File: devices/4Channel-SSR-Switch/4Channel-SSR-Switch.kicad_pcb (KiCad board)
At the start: 2 copper layers, 46 x 91.3 mm, 24 parts, among them J1 RJ45, J2 RJ45, P1 CONN_02X05, P2 CONN_01X05, P3 CONN_01X05, P4 CONN_01X05, P6 CONN_01X05, U1 LP2950, U2 STM32F030R8, U3 G3MB_SSR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

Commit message: Big cleanup/upgrade of Kicad files
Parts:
- removed G***: OSHW-logo_silkscreen-front_6mm, OSHW Logo:OSHW-logo_silkscreen-front_6mm
- added D1: SMF05C, SMF05C:SC70-6, F.Cu at (145.0, 138.8)
- added ZD1: DS9503, DS9503:TSOC6, F.Cu at (150.6, 138.2)
- moved C3 1.88 mm to (146.3, 109.5), turned to 180 degrees
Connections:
- J1 pad 1: GND -> Net-(J1-Pad1)
- J1 pad 3: GND -> Net-(J1-Pad1)
- J1 pad 4: /1W-DATA -> Net-(J1-Pad4)
- J1 pad 5: GND -> Net-(J1-Pad1)
- J1 pad 8: GND -> Net-(J1-Pad1)
- J1 pad 9: GND -> Net-(J1-Pad1)
- J2 pad 1: GND -> Net-(J1-Pad1)
- J2 pad 3: GND -> Net-(J1-Pad1)
- J2 pad 4: /1W-DATA -> Net-(J1-Pad4)
- J2 pad 5: GND -> Net-(J1-Pad1)
- J2 pad 8: GND -> Net-(J1-Pad1)
- J2 pad 9: GND -> Net-(J1-Pad1)
- P1 pad 6: (no net) -> Net-(P1-Pad6)
- P1 pad 7: (no net) -> Net-(P1-Pad7)
- P1 pad 8: (no net) -> Net-(P1-Pad8)
- U2 pad 11: (no net) -> Net-(U2-Pad11)
- U2 pad 15: (no net) -> Net-(U2-Pad15)
- U2 pad 18: (no net) -> Net-(U2-Pad18)
- U2 pad 2: (no net) -> Net-(U2-Pad2)
- U2 pad 20: (no net) -> Net-(U2-Pad20)
- U2 pad 22: (no net) -> Net-(U2-Pad22)
- U2 pad 24: (no net) -> Net-(U2-Pad24)
- U2 pad 26: (no net) -> Net-(U2-Pad26)
- U2 pad 28: (no net) -> Net-(U2-Pad28)
- U2 pad 29: (no net) -> Net-(U2-Pad29)
- U2 pad 3: (no net) -> Net-(U2-Pad3)
- U2 pad 30: (no net) -> Net-(U2-Pad30)
- U2 pad 33: (no net) -> Net-(U2-Pad33)
- U2 pad 34: (no net) -> Net-(U2-Pad34)
- U2 pad 35: (no net) -> Net-(U2-Pad35)
- U2 pad 36: (no net) -> Net-(U2-Pad36)
- U2 pad 37: (no net) -> Net-(U2-Pad37)
- U2 pad 38: (no net) -> Net-(U2-Pad38)
- U2 pad 39: (no net) -> Net-(U2-Pad39)
- U2 pad 4: (no net) -> Net-(U2-Pad4)
- U2 pad 40: (no net) -> Net-(U2-Pad40)
- U2 pad 41: (no net) -> Net-(U2-Pad41)
- U2 pad 42: (no net) -> Net-(U2-Pad42)
- U2 pad 43: (no net) -> Net-(U2-Pad43)
- U2 pad 44: (no net) -> Net-(U2-Pad44)
- U2 pad 45: (no net) -> Net-(U2-Pad45)
- U2 pad 47: (no net) -> Net-(U2-Pad47)
- U2 pad 48: (no net) -> Net-(U2-Pad48)
- U2 pad 50: (no net) -> Net-(U2-Pad50)
- U2 pad 51: (no net) -> Net-(U2-Pad51)
- U2 pad 52: (no net) -> Net-(U2-Pad52)
- U2 pad 53: (no net) -> Net-(U2-Pad53)
- U2 pad 56: (no net) -> Net-(U2-Pad56)
- U2 pad 58: (no net) -> Net-(U2-Pad58)
- U2 pad 6: (no net) -> Net-(U2-Pad6)
- U2 pad 61: (no net) -> Net-(U2-Pad61)
- U2 pad 9: (no net) -> Net-(U2-Pad9)
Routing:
- net Net-(J1-Pad1): track 0.00 -> 78.1 mm
- net GND: track 195.3 -> 131.0 mm, vias 0 -> 3
- net +5V: track 88.1 -> 147.4 mm, vias 0 -> 1
- net Net-(J1-Pad4): track 0.00 -> 33.1 mm
- net /SW2: track 58.9 -> 39.5 mm, vias 2 -> 0
- net /SWCLK: track 44.8 -> 29.3 mm
- net /1W-DATA: track 58.7 -> 43.5 mm, vias 3 -> 0
- net Net-(P2-Pad5): track 27.5 -> 17.5 mm, vias 0 -> 1
- net /OUT1: track 7.76 -> 15.5 mm
- net /SWDAT: track 21.1 -> 26.5 mm
- net +3V3: track 105.7 -> 100.8 mm
- net Net-(P2-Pad3): track 18.7 -> 15.1 mm, vias 0 -> 1
- net /SW3: track 17.6 -> 20.0 mm, vias 2 -> 0
- net Net-(P1-Pad10): track 35.2 -> 33.3 mm
- net /SW7: track 10.7 -> 12.6 mm, vias 2 -> 0
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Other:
- board text added: "1 Wire 4 Channel SSR Ver. 1.0"
- board text removed: "1 Wire 4 Channer SSR Ver. 1.0"

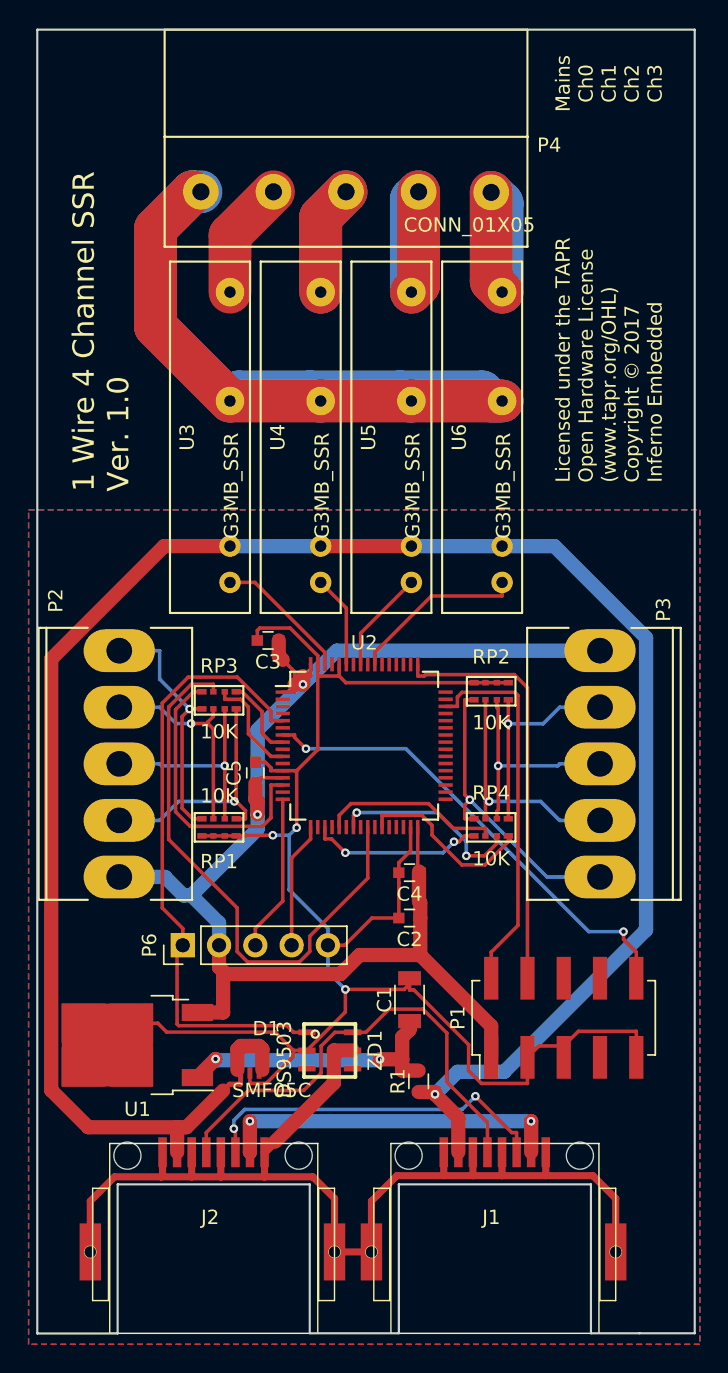
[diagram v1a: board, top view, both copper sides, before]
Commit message: Bump all active boards to Revision 1.2
- Remove dropping resistor from 5V power line
- Add pullup resistor to Reset line
- Add pin markings to STM32 chip footprint

Signed-off-by: Alastair D'Silva <alastair@d-silva.org>
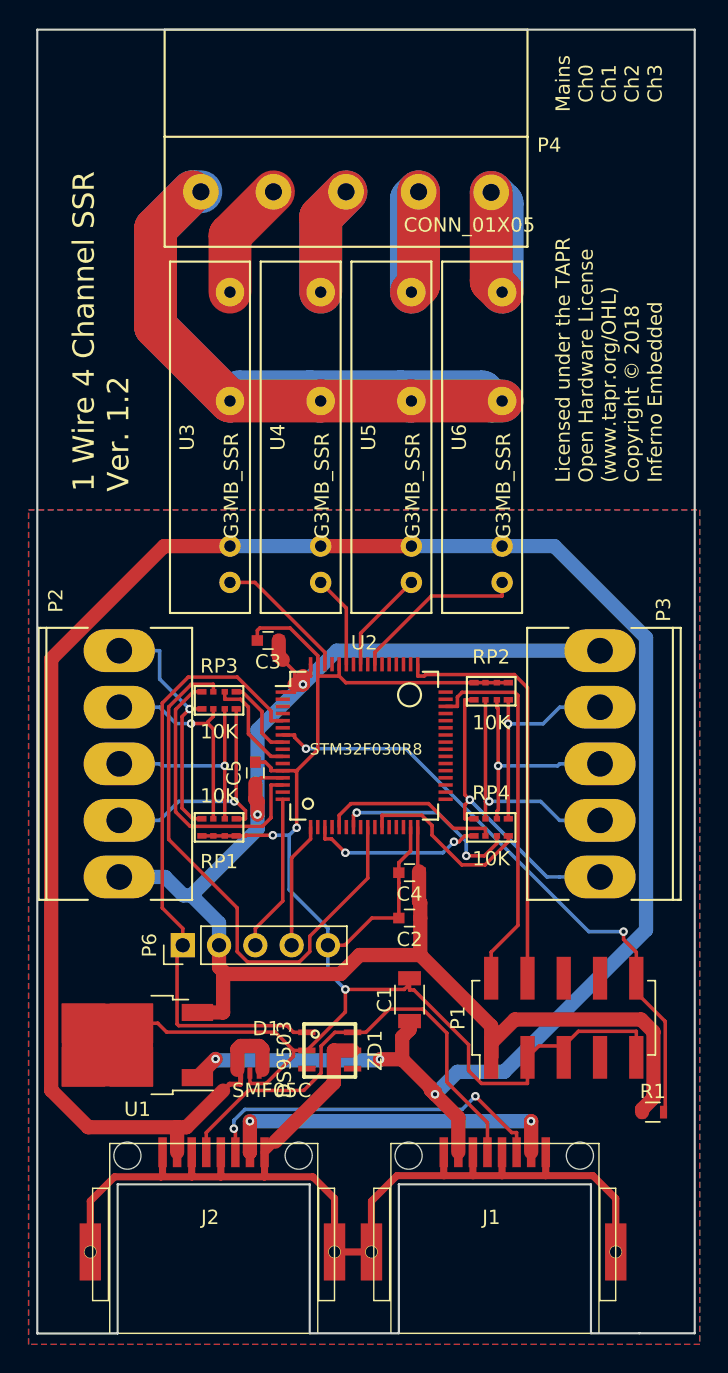
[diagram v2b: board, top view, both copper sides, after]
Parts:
- R1: value 33R -> 10k
- moved R1 16.5 mm to (173.2, 142.5), turned to 0 degrees
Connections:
- C1 pad 1: Net-(C1-Pad1) -> +5V
- R1 pad 1: +5V -> +3V3
- R1 pad 2: Net-(C1-Pad1) -> Net-(P1-Pad10)
- U1 pad 1: Net-(C1-Pad1) -> +5V
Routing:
- net +5V: track 147.4 -> 167.5 mm, vias 1 -> 3
- net Net-(C1-Pad1): track 19.8 -> 0.00 mm, vias 2 -> 0
- net +3V3: track 100.8 -> 120.1 mm
- net Net-(P1-Pad10): track 33.3 -> 43.5 mm
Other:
- board text added: "1 Wire 4 Channel SSR Ver. 1.2"
- board text added: "Licensed under the TAPR Open Hardware License (www.tapr.org/OHL) Copyright © 2018 Inferno Embedded"
- board text removed: "1 Wire 4 Channel SSR Ver. 1.0"
- board text removed: "Licensed under the TAPR Open Hardware License (www.tapr.org/OHL) Copyright © 2017 Inferno Embedded"
